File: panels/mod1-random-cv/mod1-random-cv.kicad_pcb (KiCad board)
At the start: 2 copper layers, 19.8 x 128.5 mm, 0 parts

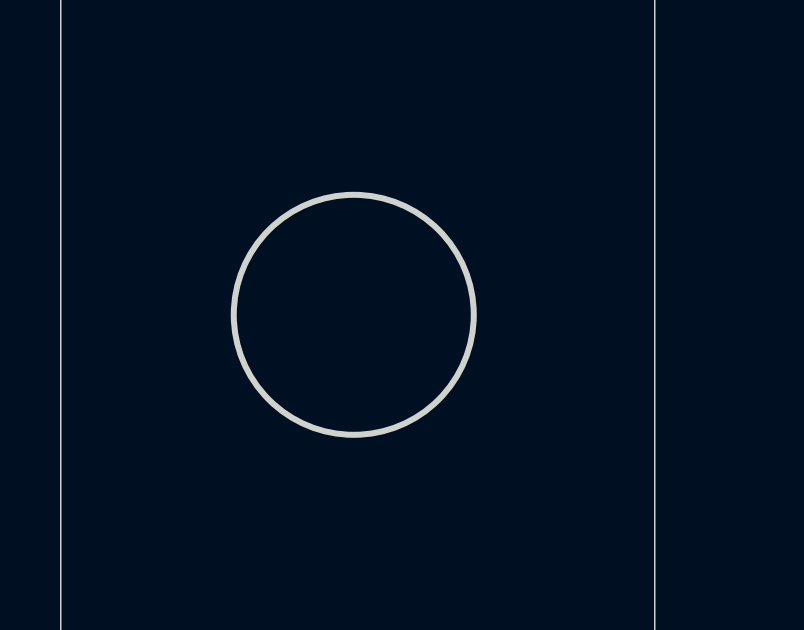
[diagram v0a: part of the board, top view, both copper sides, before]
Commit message: move vcvrack, update faceplates
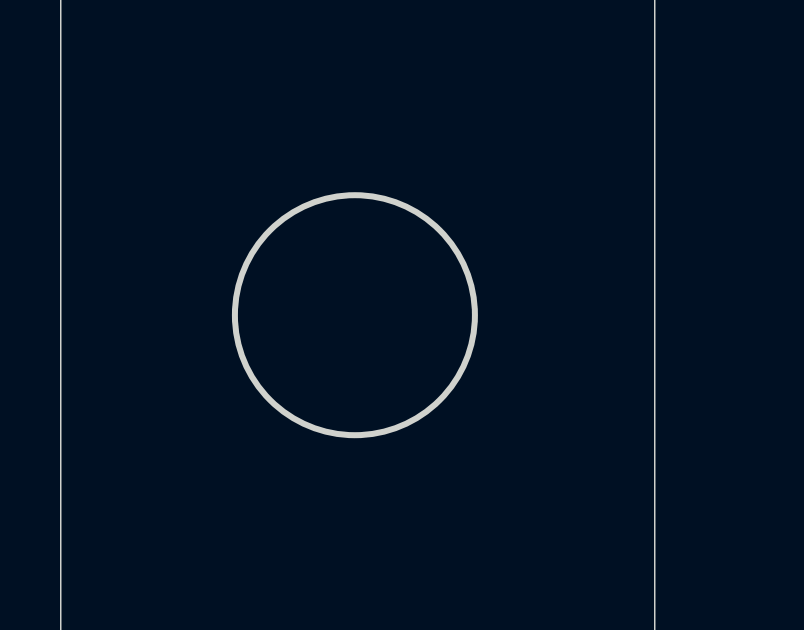
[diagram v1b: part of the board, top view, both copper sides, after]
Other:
- board text added: "16"
- board text added: "3"
- board text added: "32"
- board text added: "4"
- board text added: "5"
- board text added: "8"
- board text added: "Probability"
- board text added: "Rnd"
- board text added: "output"
- board text added: "rnd update"
- board text removed: "Prob"
- board text removed: "Update"
- board text removed: "cv"
- board text removed: "update"
